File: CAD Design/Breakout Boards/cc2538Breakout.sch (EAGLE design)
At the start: 30 parts

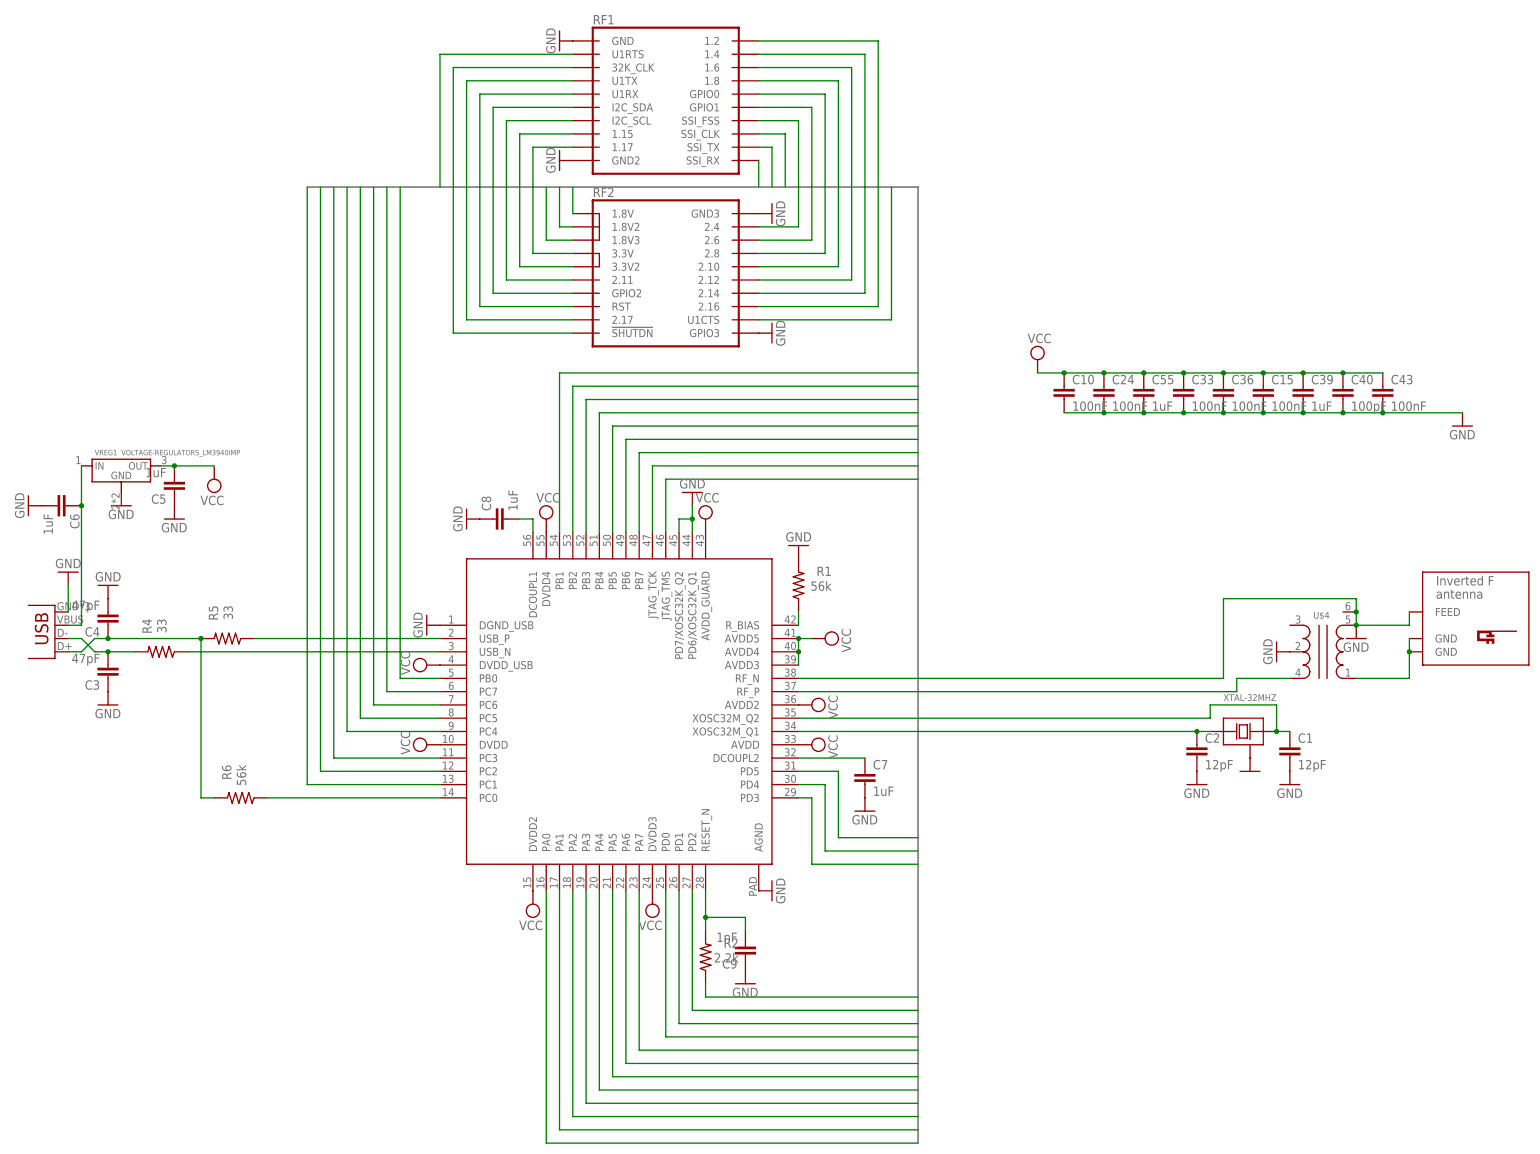
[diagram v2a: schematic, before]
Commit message: cc2538 Breakout, Board Layout upload1
Partial routing on microprocessor breakout, fixed wiring in antennae.
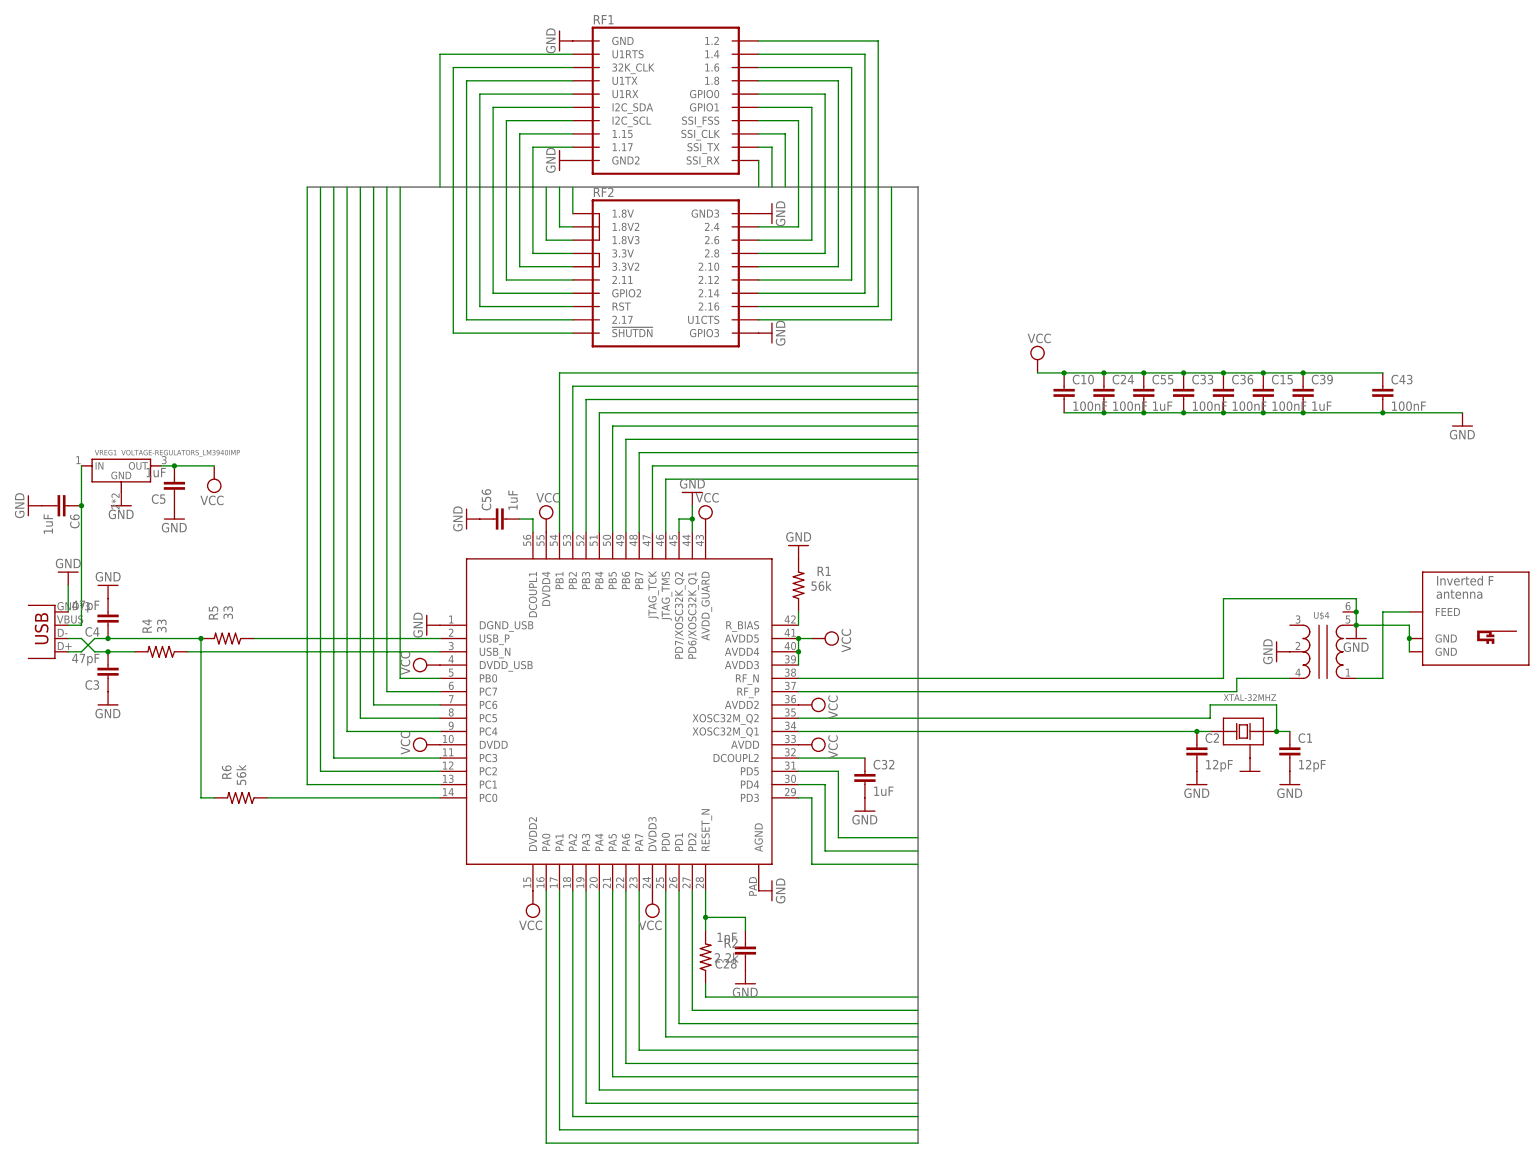
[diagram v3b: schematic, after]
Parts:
- removed C40: 100pF, resistor:C-EUC0805
- U$1: value IC_CC2538 -> CC2538; device PCB 3.0.0:IC_CC2538 -> cc2538ext:CC2538
- renumbered C7 to C32, C8 to C56, C9 to C28
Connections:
- net GND: now also U$2.GND, U$2.GND@1; no longer C40.2, U$2.FEED
- net N$2: now also U$2.FEED; no longer U$2.GND, U$2.GND@1
- net VCC: no longer C40.1
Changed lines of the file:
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@@
 </classes>
 <parts>
-<part name="U$1" library="PCB 3.0.0" deviceset="IC_CC2538" device=""/>
+<part name="U$1" library="cc2538ext" deviceset="CC2538" device=""/>
 <part name="U$2" library="PCB 3.0.0" deviceset="ANTENNA_INVERTED_F_ANTENNA" device="+0"/>
 <part name="XTAL-32MHZ" library="PCB 3.0.0" deviceset="DISCRETE_XTAL-4" device="3225"/>
@@
 <part name="GND18" library="supply1" deviceset="GND" device=""/>
 <part name="C1" library="resistor" deviceset="C-EU" device="C0805" value="12pF"/>
-<part name="C7" library="resistor" deviceset="C-EU" device="C0805" value="1uF"/>
-<part name="C8" library="resistor" deviceset="C-EU" device="C0805" value="1uF"/>
-<part name="C9" library="resistor" deviceset="C-EU" device="C0805" value="1nF"/>
+<part name="C32" library="resistor" deviceset="C-EU" device="C0805" value="1uF"/>
+<part name="C56" library="resistor" deviceset="C-EU" device="C0805" value="1uF"/>
+<part name="C28" library="resistor" deviceset="C-EU" device="C0805" value="1nF"/>
 <part name="C3" library="resistor" deviceset="C-EU" device="C0805" value="47pF"/>
 <part name="C4" library="resistor" deviceset="C-EU" device="C0805" value="47pF"/>
@@
 <part name="C15" library="resistor" deviceset="C-EU" device="C0805" value="100nF"/>
 <part name="C39" library="resistor" deviceset="C-EU" device="C0805" value="1uF"/>
-<part name="C40" library="resistor" deviceset="C-EU" device="C0805" value="100pF"/>
 <part name="C43" library="resistor" deviceset="C-EU" device="C0805" value="100nF"/>
 <part name="SUPPLY11" library="supply2" deviceset="VCC" device=""/>
@@
 <instance part="GND18" gate="1" x="2.54" y="119.38" rot="R270"/>
 <instance part="C1" gate="G$1" x="243.84" y="73.66"/>
-<instance part="C7" gate="G$1" x="162.56" y="68.58"/>
-<instance part="C8" gate="G$1" x="91.44" y="116.84" rot="R90"/>
-<instance part="C9" gate="G$1" x="139.7" y="33.02" rot="R180"/>
+<instance part="C32" gate="G$1" x="162.56" y="68.58"/>
+<instance part="C56" gate="G$1" x="91.44" y="116.84" rot="R90"/>
+<instance part="C28" gate="G$1" x="139.7" y="33.02" rot="R180"/>
 <instance part="C3" gate="G$1" x="17.78" y="86.36" rot="R180"/>
 <instance part="C4" gate="G$1" x="17.78" y="96.52" rot="R180"/>
@@
 <instance part="C15" gate="G$1" x="238.76" y="142.24"/>
 <instance part="C39" gate="G$1" x="246.38" y="142.24"/>
-<instance part="C40" gate="G$1" x="254" y="142.24"/>
 <instance part="C43" gate="G$1" x="261.62" y="142.24"/>
 <instance part="SUPPLY11" gate="G$1" x="195.58" y="147.32"/>
@@
 <segment>
 <pinref part="U$1" gate="G$1" pin="RF_N"/>
-<pinref part="U$2" gate="G$1" pin="FEED"/>
-<wire x1="266.7" y1="99.06" x2="266.7" y2="96.52" width="0.1524" layer="91"/>
 <pinref part="U$4" gate="G$1" pin="5"/>
-<wire x1="266.7" y1="96.52" x2="256.54" y2="96.52" width="0.1524" layer="91"/>
 <wire x1="256.54" y1="96.52" x2="256.54" y2="99.06" width="0.1524" layer="91"/>
 <wire x1="256.54" y1="99.06" x2="256.54" y2="101.6" width="0.1524" layer="91"/>
@@
 <pinref part="U$4" gate="G$1" pin="6"/>
 <junction x="256.54" y="99.06"/>
+<pinref part="U$2" gate="G$1" pin="GND"/>
+<wire x1="266.7" y1="93.98" x2="266.7" y2="91.44" width="0.1524" layer="91"/>
+<pinref part="U$2" gate="G$1" pin="GND@1"/>
+<wire x1="266.7" y1="93.98" x2="266.7" y2="96.52" width="0.1524" layer="91"/>
+<wire x1="266.7" y1="96.52" x2="256.54" y2="96.52" width="0.1524" layer="91"/>
+<junction x="266.7" y="93.98"/>
 </segment>
 <segment>
@@
 <segment>
 <pinref part="GND4" gate="1" pin="GND"/>
-<pinref part="C7" gate="G$1" pin="2"/>
+<pinref part="C32" gate="G$1" pin="2"/>
 </segment>
 <segment>
 <pinref part="GND2" gate="1" pin="GND"/>
-<pinref part="C8" gate="G$1" pin="1"/>
+<pinref part="C56" gate="G$1" pin="1"/>
 </segment>
 <segment>
 <pinref part="GND6" gate="1" pin="GND"/>
-<pinref part="C9" gate="G$1" pin="1"/>
+<pinref part="C28" gate="G$1" pin="1"/>
 </segment>
 <segment>
@@
 <wire x1="231.14" y1="137.16" x2="238.76" y2="137.16" width="0.1524" layer="91"/>
 <wire x1="238.76" y1="137.16" x2="246.38" y2="137.16" width="0.1524" layer="91"/>
-<wire x1="246.38" y1="137.16" x2="254" y2="137.16" width="0.1524" layer="91"/>
-<wire x1="254" y1="137.16" x2="261.62" y2="137.16" width="0.1524" layer="91"/>
+<wire x1="246.38" y1="137.16" x2="261.62" y2="137.16" width="0.1524" layer="91"/>
 <wire x1="261.62" y1="137.16" x2="276.86" y2="137.16" width="0.1524" layer="91"/>
 <pinref part="C43" gate="G$1" pin="2"/>
 <junction x="261.62" y="137.16"/>
-<pinref part="C40" gate="G$1" pin="2"/>
-<junction x="254" y="137.16"/>
 <pinref part="C39" gate="G$1" pin="2"/>
 <junction x="246.38" y="137.16"/>
@@
 <wire x1="99.06" y1="114.3" x2="99.06" y2="116.84" width="0.1524" layer="91"/>
 <wire x1="99.06" y1="116.84" x2="96.52" y2="116.84" width="0.1524" layer="91"/>
-<pinref part="C8" gate="G$1" pin="2"/>
+<pinref part="C56" gate="G$1" pin="2"/>
 </segment>
 </net>
@@
 <pinref part="U$1" gate="G$1" pin="DCOUPL2"/>
 <wire x1="149.86" y1="71.12" x2="162.56" y2="71.12" width="0.1524" layer="91"/>
-<pinref part="C7" gate="G$1" pin="1"/>
+<pinref part="C32" gate="G$1" pin="1"/>
 </segment>
 </net>
@@
 <wire x1="139.7" y1="40.64" x2="139.7" y2="38.1" width="0.1524" layer="91"/>
 <junction x="132.08" y="40.64"/>
-<pinref part="C9" gate="G$1" pin="2"/>
+<pinref part="C28" gate="G$1" pin="2"/>
 <pinref part="R2" gate="G$1" pin="2"/>
-</segment>
-</net>
-<net name="N$2" class="0">
-<segment>
-<pinref part="U$2" gate="G$1" pin="GND"/>
-<wire x1="266.7" y1="93.98" x2="266.7" y2="91.44" width="0.1524" layer="91"/>
-<pinref part="U$4" gate="G$1" pin="1"/>
-<wire x1="266.7" y1="91.44" x2="266.7" y2="86.36" width="0.1524" layer="91"/>
-<wire x1="266.7" y1="86.36" x2="256.54" y2="86.36" width="0.1524" layer="91"/>
-<pinref part="U$2" gate="G$1" pin="GND@1"/>
-<junction x="266.7" y="91.44"/>
 </segment>
 </net>
@@
 <junction x="238.76" y="144.78"/>
 <pinref part="C39" gate="G$1" pin="1"/>
-<wire x1="246.38" y1="144.78" x2="254" y2="144.78" width="0.1524" layer="91"/>
 <junction x="246.38" y="144.78"/>
-<pinref part="C40" gate="G$1" pin="1"/>
-<wire x1="254" y1="144.78" x2="261.62" y2="144.78" width="0.1524" layer="91"/>
-<junction x="254" y="144.78"/>
+<wire x1="246.38" y1="144.78" x2="261.62" y2="144.78" width="0.1524" layer="91"/>
 <pinref part="C43" gate="G$1" pin="1"/>
 <pinref part="SUPPLY11" gate="G$1" pin="VCC"/>
@@
 </segment>
 </net>
+<net name="N$2" class="0">
+<segment>
+<pinref part="U$2" gate="G$1" pin="FEED"/>
+<wire x1="266.7" y1="99.06" x2="261.62" y2="99.06" width="0.1524" layer="91"/>
+<wire x1="261.62" y1="99.06" x2="261.62" y2="86.36" width="0.1524" layer="91"/>
+<pinref part="U$4" gate="G$1" pin="1"/>
+<wire x1="261.62" y1="86.36" x2="256.54" y2="86.36" width="0.1524" layer="91"/>
+</segment>
+</net>

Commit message: cc2538 breakout. update#2
Routed antennae, better xtal routing. Most of power routed. I/O still
to come.
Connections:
- new net ANT_GND: U$1.RF_N, U$2.GND, U$2.GND@1, U$4.5, U$4.6
- net GND: no longer U$1.RF_N, U$2.GND, U$2.GND@1, U$4.5, U$4.6
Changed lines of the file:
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@@
 <part name="GND9" library="supply1" deviceset="GND" device=""/>
 <part name="GND10" library="supply1" deviceset="GND" device=""/>
-<part name="GND11" library="supply1" deviceset="GND" device=""/>
+<part name="GND" library="supply1" deviceset="GND" device=""/>
 <part name="SUPPLY1" library="supply2" deviceset="VCC" device=""/>
 <part name="SUPPLY2" library="supply2" deviceset="VCC" device=""/>
@@
 <part name="C43" library="resistor" deviceset="C-EU" device="C0805" value="100nF"/>
 <part name="SUPPLY11" library="supply2" deviceset="VCC" device=""/>
-<part name="GND23" library="supply1" deviceset="GND" device=""/>
+<part name="CPU_GND" library="supply1" deviceset="GND" device=""/>
 </parts>
 <sheets>
@@
 <instance part="GND9" gate="1" x="243.84" y="66.04"/>
 <instance part="GND10" gate="1" x="256.54" y="93.98"/>
-<instance part="GND11" gate="1" x="241.3" y="91.44" rot="R270"/>
+<instance part="GND" gate="1" x="241.3" y="91.44" rot="R270"/>
 <instance part="SUPPLY1" gate="G$1" x="154.94" y="93.98" rot="R270"/>
 <instance part="SUPPLY2" gate="G$1" x="152.4" y="81.28" rot="R270"/>
@@
 <instance part="C43" gate="G$1" x="261.62" y="142.24"/>
 <instance part="SUPPLY11" gate="G$1" x="195.58" y="147.32"/>
-<instance part="GND23" gate="1" x="276.86" y="134.62"/>
+<instance part="CPU_GND" gate="1" x="276.86" y="134.62"/>
 </instances>
 <busses>
@@
 </segment>
 <segment>
-<pinref part="U$1" gate="G$1" pin="RF_N"/>
-<pinref part="U$4" gate="G$1" pin="5"/>
-<wire x1="256.54" y1="96.52" x2="256.54" y2="99.06" width="0.1524" layer="91"/>
-<wire x1="256.54" y1="99.06" x2="256.54" y2="101.6" width="0.1524" layer="91"/>
-<wire x1="256.54" y1="101.6" x2="231.14" y2="101.6" width="0.1524" layer="91"/>
-<wire x1="231.14" y1="101.6" x2="231.14" y2="86.36" width="0.1524" layer="91"/>
-<wire x1="231.14" y1="86.36" x2="149.86" y2="86.36" width="0.1524" layer="91"/>
-<junction x="256.54" y="96.52"/>
-<pinref part="GND10" gate="1" pin="GND"/>
-<pinref part="U$4" gate="G$1" pin="6"/>
-<junction x="256.54" y="99.06"/>
-<pinref part="U$2" gate="G$1" pin="GND"/>
-<wire x1="266.7" y1="93.98" x2="266.7" y2="91.44" width="0.1524" layer="91"/>
-<pinref part="U$2" gate="G$1" pin="GND@1"/>
-<wire x1="266.7" y1="93.98" x2="266.7" y2="96.52" width="0.1524" layer="91"/>
-<wire x1="266.7" y1="96.52" x2="256.54" y2="96.52" width="0.1524" layer="91"/>
-<junction x="266.7" y="93.98"/>
-</segment>
-<segment>
 <pinref part="U$4" gate="G$1" pin="2"/>
-<pinref part="GND11" gate="1" pin="GND"/>
+<pinref part="GND" gate="1" pin="GND"/>
 </segment>
 <segment>
@@
 <pinref part="C10" gate="G$1" pin="2"/>
 <wire x1="200.66" y1="137.16" x2="208.28" y2="137.16" width="0.1524" layer="91"/>
-<pinref part="GND23" gate="1" pin="GND"/>
+<pinref part="CPU_GND" gate="1" pin="GND"/>
 <wire x1="208.28" y1="137.16" x2="215.9" y2="137.16" width="0.1524" layer="91"/>
 <wire x1="215.9" y1="137.16" x2="223.52" y2="137.16" width="0.1524" layer="91"/>
@@
 </segment>
 </net>
+<net name="ANT_GND" class="0">
+<segment>
+<pinref part="U$1" gate="G$1" pin="RF_N"/>
+<pinref part="U$4" gate="G$1" pin="5"/>
+<wire x1="256.54" y1="96.52" x2="256.54" y2="99.06" width="0.1524" layer="91"/>
+<wire x1="256.54" y1="99.06" x2="256.54" y2="101.6" width="0.1524" layer="91"/>
+<wire x1="256.54" y1="101.6" x2="231.14" y2="101.6" width="0.1524" layer="91"/>
+<wire x1="231.14" y1="101.6" x2="231.14" y2="86.36" width="0.1524" layer="91"/>
+<wire x1="231.14" y1="86.36" x2="149.86" y2="86.36" width="0.1524" layer="91"/>
+<junction x="256.54" y="96.52"/>
+<pinref part="GND10" gate="1" pin="GND"/>
+<pinref part="U$4" gate="G$1" pin="6"/>
+<junction x="256.54" y="99.06"/>
+<pinref part="U$2" gate="G$1" pin="GND"/>
+<wire x1="266.7" y1="93.98" x2="266.7" y2="91.44" width="0.1524" layer="91"/>
+<pinref part="U$2" gate="G$1" pin="GND@1"/>
+<wire x1="266.7" y1="93.98" x2="266.7" y2="96.52" width="0.1524" layer="91"/>
+<wire x1="266.7" y1="96.52" x2="256.54" y2="96.52" width="0.1524" layer="91"/>
+<junction x="266.7" y="93.98"/>
+</segment>
+</net>

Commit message: cc2538 Breakout_rev1.0
cc2538 Breakout board ready to go to print. Fixed crossed signals on
PC0/PC1, verified headers, second and third DRC’s passed.
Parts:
- R6: value 56k -> 1.5k
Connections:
- net I/O31: no longer U$1.PC1
- net I/O33: now also U$1.PC1
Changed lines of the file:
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@@
 <part name="R4" library="resistor" deviceset="R-US_" device="R0805" value="33"/>
 <part name="R5" library="resistor" deviceset="R-US_" device="R0805" value="33"/>
-<part name="R6" library="resistor" deviceset="R-US_" device="R0805" value="56k"/>
+<part name="R6" library="resistor" deviceset="R-US_" device="R0805" value="1.5k"/>
 <part name="GND7" library="supply1" deviceset="GND" device=""/>
 <part name="GND19" library="supply1" deviceset="GND" device=""/>
@@
 <wire x1="93.98" y1="162.56" x2="93.98" y2="180.34" width="0.1524" layer="91"/>
 </segment>
+</net>
+<net name="I/O33" class="0">
+<segment>
+<pinref part="U$3" gate="G$1" pin="GPIO2"/>
+<wire x1="106.68" y1="160.02" x2="91.44" y2="160.02" width="0.1524" layer="91"/>
+<wire x1="91.44" y1="160.02" x2="91.44" y2="180.34" width="0.1524" layer="91"/>
+</segment>
 <segment>
 <pinref part="U$1" gate="G$1" pin="PC1"/>
@@
 </segment>
 </net>
-<net name="I/O33" class="0">
-<segment>
-<pinref part="U$3" gate="G$1" pin="GPIO2"/>
-<wire x1="106.68" y1="160.02" x2="91.44" y2="160.02" width="0.1524" layer="91"/>
-<wire x1="91.44" y1="160.02" x2="91.44" y2="180.34" width="0.1524" layer="91"/>
-</segment>
-</net>
